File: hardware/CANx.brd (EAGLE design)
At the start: 53.3 x 30.5 mm, 13 parts, among them Q1 16MHz, U9 MCP2551SO8, X2 RJ45_RIGHT_ANGLEMOLEX_95001-2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, X4 RJ45_RIGHT_ANGLEMOLEX_95001-2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

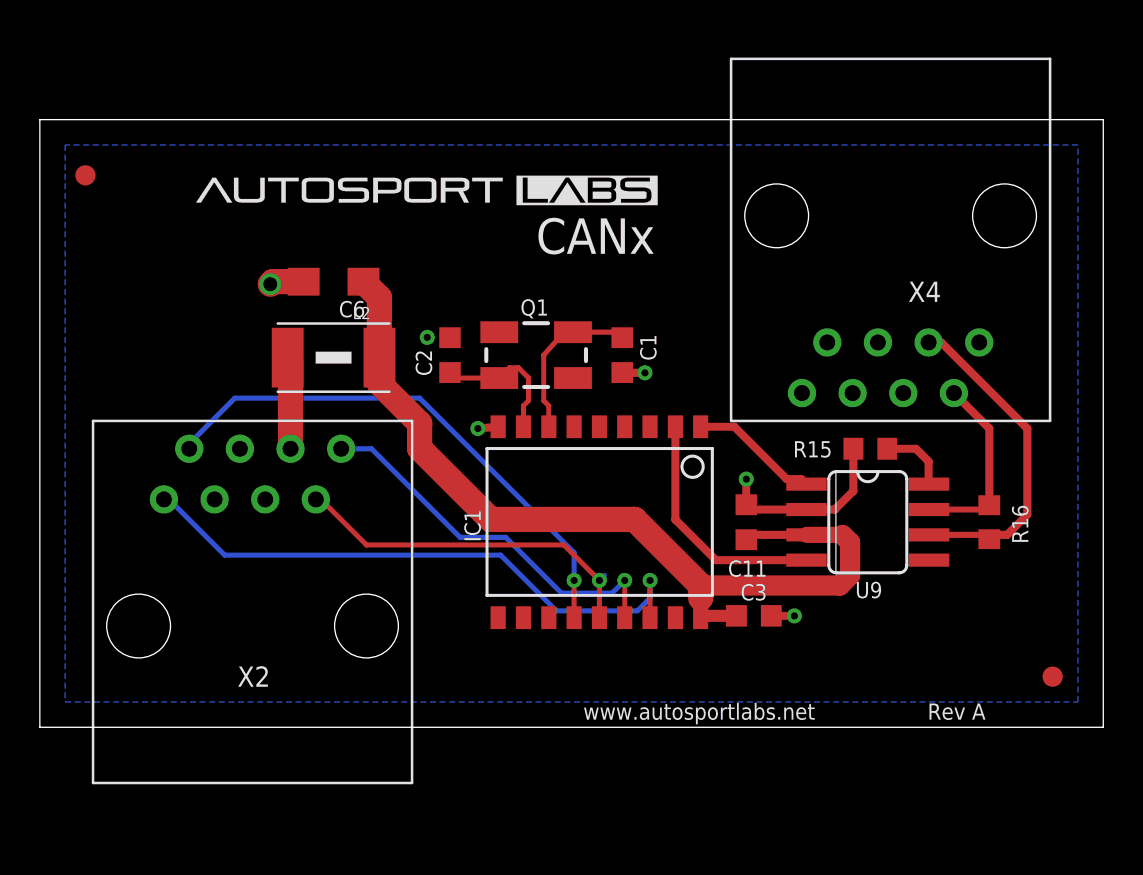
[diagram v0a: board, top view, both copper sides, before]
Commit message: shrunk design of design to fit same enclosure as BT module
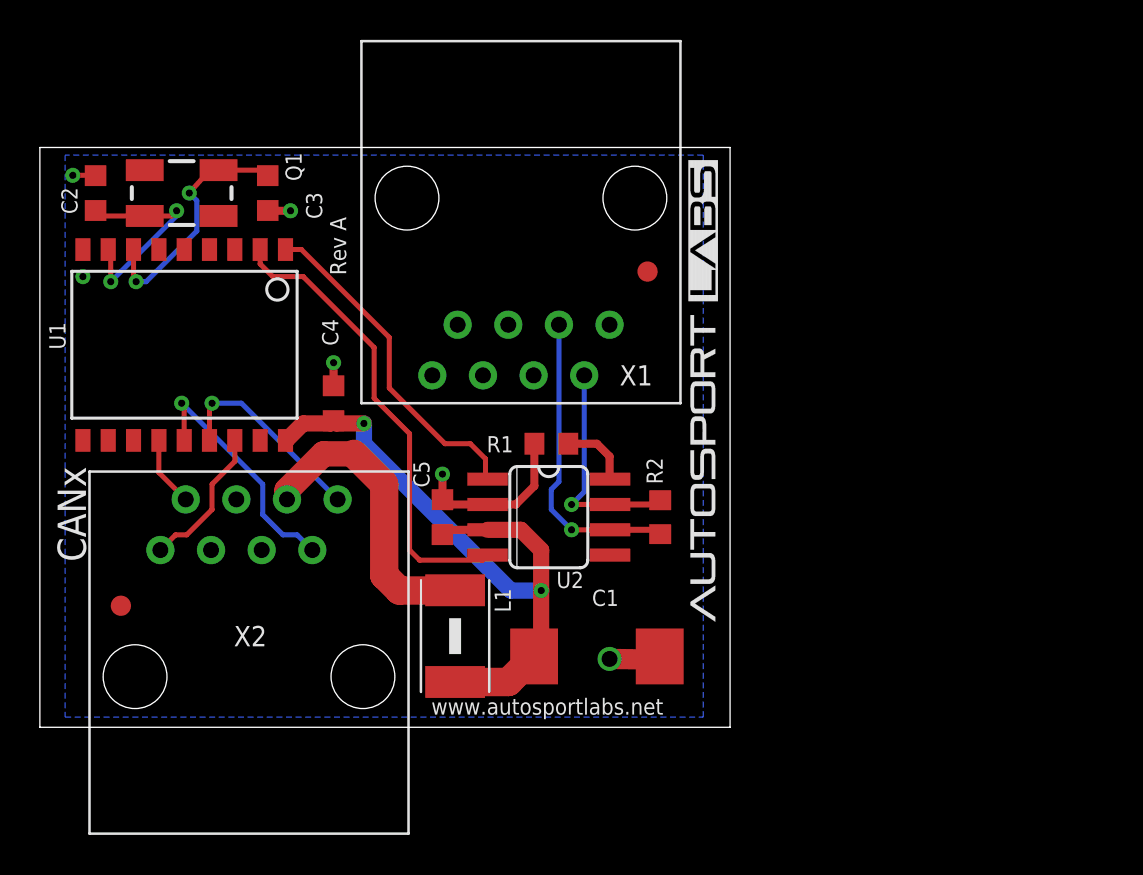
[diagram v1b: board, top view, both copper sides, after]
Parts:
- removed C11: 0.1uf, rcl:C0603K
- removed C6: 10uF, rcl:SMC_A
- removed IC1: (no value), can:SO-18W
- removed L2: (no value), wuerth-elektronik:1812
- removed R15: 4.7K, rcl:R0603
- removed R16: 120, rcl:R0603
- removed U9: MCP2551SO8, can:SO08
- removed X4: RJ45_RIGHT_ANGLEMOLEX_95001-2881, FCI_RJ12:RJ45_RIGHT_ANGLE_MOLEX_95001-2881
- added C4: 0.1uF, rcl:C0603K
- added C5: 0.1uf, rcl:C0603K
- added L1: (no value), wuerth-elektronik:1812
- added R1: 4.7K, rcl:R0603
- added R2: 120, rcl:R0603
- added U1: (no value), can:SO-18W
- added U2: MCP2551SO8, can:SO08
- added X1: RJ45_RIGHT_ANGLEMOLEX_95001-2881, FCI_RJ12:RJ45_RIGHT_ANGLE_MOLEX_95001-2881
- C1: value 22pF -> 10uF; device rcl:C0603K -> rcl:SMC_D
- C3: value 0.1uF -> 22pF
- moved C3 32.3 mm to (11.4, 26.8), turned to 270 degrees
- moved C2 19.5 mm to (2.79, 26.8)
- moved Q1 19.5 mm to (7.11, 26.8)
- moved C1 15.2 mm to (27.9, 3.56), turned to 0 degrees
- moved X2 2.55 mm to (10.5, 2.54)
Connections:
- net +12V: now also X1.P8; no longer X4.P8
- net +5V: now also C1.+, C4.1, C5.1, L1.1, U1.18, U2.3; no longer C11.1, C3.1, C6.+, IC1.18, L2.1, U9.3
- net CAN1_RX: now also U1.2, U2.4; no longer IC1.2, U9.4
- net CAN1_TX: now also U1.1, U2.1; no longer IC1.1, U9.1
- net CANH: now also R2.1, U2.7, X1.P2; no longer R16.1, U9.7, X4.P2
- net CANL: now also R2.2, U2.6, X1.P3; no longer R16.2, U9.6, X4.P3
- net GND: now also C1.-, C4.2, C5.2, R1.1, U1.9, U2.2, X1.P1; no longer C1.2, C11.2, C6.-, IC1.9, R15.1, U9.2, X4.P1
- net MISO: now also U1.15; no longer IC1.15
- net MOSI: now also U1.14; no longer IC1.14
- net N$1: now also U1.8; no longer IC1.8
- net N$2: now also C3.1, U1.7; no longer C1.1, IC1.7
- net N$34: now also R1.2, U2.8; no longer R15.2, U9.8
- net N$4: now also L1.2; no longer L2.2
- net NPCS1: now also U1.16; no longer IC1.16
- net SPCK: now also U1.13; no longer IC1.13
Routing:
- net SPCK: track 27.0 -> 3.52 mm, vias 1 -> 0
- net NPCS1: track 29.7 -> 7.37 mm, vias 1 -> 0
- net +5V: track 44.9 -> 32.6 mm, vias 0 -> 2
- net CAN1_RX: track 12.1 -> 23.3 mm
- net N$4: track 4.63 -> 15.2 mm
- net CAN1_TX: track 6.50 -> 16.9 mm
- net MISO: track 19.4 -> 10.2 mm
- net MOSI: track 18.1 -> 12.4 mm
- net N$2: track 8.27 -> 12.4 mm, vias 0 -> 2
- net N$1: track 7.08 -> 10.9 mm, vias 0 -> 2
- net CANH: track 9.60 -> 12.0 mm, vias 0 -> 1
- net CANL: track 16.6 -> 16.8 mm, vias 0 -> 1
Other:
- board size 53.3 x 30.5 mm -> 34.6 x 29.1 mm
